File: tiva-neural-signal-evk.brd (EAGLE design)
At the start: 100 x 80 mm, 32 parts, among them IC1 TM4C123G, IC2 TLV70233, X1 USB, Y1 16MHz, Y2 32.768kHz

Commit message: added SD card in SPI mode
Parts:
- added C17: 0.1uF, rcl:C0603
- added X2: MICROSD, mor307:PUSH-PUSH
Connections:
- net +3V3: now also C17.1, X2.4
- net GND: now also C17.2, X2.6
- net PF0: now also X2.7
- net PF1: now also X2.3
- net PF2: now also X2.5
- net PF3: now also X2.2
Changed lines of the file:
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@@
 <attribute name="TP_SIGNAL_NAME" value="" x="-52.07" y="-106.68" size="1.778" layer="27" display="off"/>
 </element>
+<element name="X2" library="mor307" package="PUSH-PUSH" value="MICROSD" x="-67.31" y="-106.68"/>
+<element name="C17" library="rcl" package="C0603" value="0.1uF" x="-66.04" y="-110.49"/>
 </elements>
 <signals>
@@
 <contactref element="S1" pad="1"/>
 <contactref element="S1" pad="2"/>
+<contactref element="X2" pad="6"/>
+<contactref element="C17" pad="2"/>
+<wire x1="-63.66" y1="-102.38" x2="-65.19" y2="-110.49" width="0" layer="19" extent="1-1"/>
+<wire x1="-51.562" y1="-89.154" x2="-63.66" y2="-102.38" width="0" layer="19" extent="1-1"/>
 <wire x1="-44.958" y1="-89.154" x2="-51.562" y2="-89.154" width="0" layer="19" extent="1-1"/>
 <wire x1="-39.79" y1="-81.28" x2="-44.958" y2="-89.154" width="0" layer="19" extent="1-1"/>
@@
 <contactref element="+3V3" pad="TP"/>
 <contactref element="R3" pad="1"/>
+<contactref element="X2" pad="4"/>
+<contactref element="C17" pad="1"/>
+<wire x1="-61.46" y1="-102.38" x2="-66.89" y2="-110.49" width="0" layer="19" extent="1-1"/>
+<wire x1="-51.65" y1="-100.33" x2="-61.46" y2="-102.38" width="0" layer="19" extent="1-1"/>
 <wire x1="-39.79" y1="-85.09" x2="-51.65" y2="-100.33" width="0" layer="19" extent="1-1"/>
 <wire x1="-36.41" y1="-41.91" x2="-39.79" y2="-85.09" width="0" layer="19" extent="1-1"/>
@@
 <signal name="PF0">
 <contactref element="IC1" pad="28"/>
+<contactref element="X2" pad="7"/>
+<wire x1="-18.57" y1="2.02" x2="-64.76" y2="-102.38" width="0" layer="19" extent="1-1"/>
 </signal>
 <signal name="PF1">
 <contactref element="IC1" pad="29"/>
+<contactref element="X2" pad="3"/>
+<wire x1="-18.07" y1="2.02" x2="-60.36" y2="-102.38" width="0" layer="19" extent="1-1"/>
 </signal>
 <signal name="PF2">
 <contactref element="IC1" pad="30"/>
+<contactref element="X2" pad="5"/>
+<wire x1="-17.57" y1="2.02" x2="-62.56" y2="-102.38" width="0" layer="19" extent="1-1"/>
 </signal>
 <signal name="PF3">
 <contactref element="IC1" pad="31"/>
+<contactref element="X2" pad="2"/>
+<wire x1="-17.07" y1="2.02" x2="-59.26" y2="-102.38" width="0" layer="19" extent="1-1"/>
 </signal>
 <signal name="PF4">

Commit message: added 2-ch instrumentation amp w/ op-amp gain stage
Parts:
- added C18: 0.1uF, rcl:C0603
- added C19, C20, C21, C22, C23, C24: (no value), rcl:C0603
- added IC3: INA2332, mor307:TSSOP16
- added IC4, IC5: OPA2320, mor307:MSOP08
- added R4, R5, R6, R7: 100k, rcl:R0603
- added R8, R9: 1M, rcl:R0603
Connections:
- new net N$1: C20.2, IC3.7, R6.1, R7.1
- new net N$12: C19.2, IC3.13, R5.2, R8.1
- new net N$14: C21.1, IC4.2, R8.2
- new net N$15: C22.2, IC5.2, R9.2
- new net N$2: C22.1, IC3.10, IC5.1, R6.2
- new net N$3: C20.1, IC3.9, R7.2, R9.1
- new net N$4: C19.1, IC3.1, R4.1, R5.1
- new net N$5: C21.2, IC3.12, IC4.1, R4.2
- net +3V3: now also C18.1, C23.1, C24.1, IC3.11, IC3.14, IC3.8, IC4.8, IC5.8
- net GND: now also C18.2, C23.2, C24.2, IC3.4, IC4.4, IC5.4
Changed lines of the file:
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@@
 <element name="X2" library="mor307" package="PUSH-PUSH" value="MICROSD" x="-67.31" y="-106.68"/>
 <element name="C17" library="rcl" package="C0603" value="0.1uF" x="-66.04" y="-110.49"/>
+<element name="IC3" library="mor307" package="TSSOP16" value="INA2332" x="-73.66" y="-107.95"/>
+<element name="IC4" library="mor307" package="MSOP08" value="OPA2320" x="-73.66" y="-116.84"/>
+<element name="IC5" library="mor307" package="MSOP08" value="OPA2320" x="-73.66" y="-124.46"/>
+<element name="C18" library="rcl" package="C0603" value="0.1uF" x="-74.93" y="-130.81"/>
+<element name="R4" library="rcl" package="R0603" value="100k" x="-74.93" y="-135.89"/>
+<element name="R5" library="rcl" package="R0603" value="100k" x="-74.93" y="-140.97"/>
+<element name="C19" library="rcl" package="C0603" value="" x="-74.93" y="-146.05"/>
+<element name="R6" library="rcl" package="R0603" value="100k" x="-74.93" y="-149.86"/>
+<element name="R7" library="rcl" package="R0603" value="100k" x="-74.93" y="-154.94"/>
+<element name="C20" library="rcl" package="C0603" value="" x="-74.93" y="-160.02"/>
+<element name="R8" library="rcl" package="R0603" value="1M" x="-74.93" y="-163.83"/>
+<element name="C21" library="rcl" package="C0603" value="" x="-74.93" y="-168.91"/>
+<element name="R9" library="rcl" package="R0603" value="1M" x="-74.93" y="-172.72"/>
+<element name="C22" library="rcl" package="C0603" value="" x="-74.93" y="-177.8"/>
+<element name="C23" library="rcl" package="C0603" value="" x="-74.93" y="-181.61"/>
+<element name="C24" library="rcl" package="C0603" value="" x="-74.93" y="-185.42"/>
 </elements>
 <signals>
@@
 <contactref element="X2" pad="6"/>
 <contactref element="C17" pad="2"/>
+<contactref element="IC3" pad="4"/>
+<contactref element="C18" pad="2"/>
+<contactref element="IC4" pad="4"/>
+<contactref element="C23" pad="2"/>
+<contactref element="IC5" pad="4"/>
+<contactref element="C24" pad="2"/>
+<wire x1="-75.773" y1="-125.434" x2="-74.08" y2="-130.81" width="0" layer="19" extent="1-1"/>
+<wire x1="-75.773" y1="-117.814" x2="-75.773" y2="-125.434" width="0" layer="19" extent="1-1"/>
+<wire x1="-76.685" y1="-107.625" x2="-75.773" y2="-117.814" width="0" layer="19" extent="1-1"/>
+<wire x1="-65.19" y1="-110.49" x2="-76.685" y2="-107.625" width="0" layer="19" extent="1-1"/>
 <wire x1="-63.66" y1="-102.38" x2="-65.19" y2="-110.49" width="0" layer="19" extent="1-1"/>
 <wire x1="-51.562" y1="-89.154" x2="-63.66" y2="-102.38" width="0" layer="19" extent="1-1"/>
@@
 <wire x1="-29.21" y1="17.7499" x2="-25.92" y2="10.37" width="0" layer="19" extent="1-1"/>
 <wire x1="-16.48" y1="22.97" x2="-19.57" y2="13.22" width="0" layer="19" extent="1-1"/>
+<wire x1="-74.08" y1="-181.61" x2="-74.08" y2="-130.81" width="0" layer="19" extent="1-1"/>
+<wire x1="-74.08" y1="-185.42" x2="-74.08" y2="-181.61" width="0" layer="19" extent="1-1"/>
 </signal>
 <signal name="VBUS">
@@
 <contactref element="X2" pad="4"/>
 <contactref element="C17" pad="1"/>
+<contactref element="IC3" pad="11"/>
+<contactref element="C18" pad="1"/>
+<contactref element="IC3" pad="14"/>
+<contactref element="IC3" pad="8"/>
+<contactref element="C23" pad="1"/>
+<contactref element="IC4" pad="8"/>
+<contactref element="IC5" pad="8"/>
+<contactref element="C24" pad="1"/>
+<wire x1="-71.548" y1="-123.484" x2="-75.78" y2="-130.81" width="0" layer="19" extent="1-1"/>
+<wire x1="-71.548" y1="-115.864" x2="-71.548" y2="-123.484" width="0" layer="19" extent="1-1"/>
+<wire x1="-70.635" y1="-108.925" x2="-71.548" y2="-115.864" width="0" layer="19" extent="1-1"/>
+<wire x1="-70.635" y1="-106.975" x2="-70.635" y2="-108.925" width="0" layer="19" extent="1-1"/>
+<wire x1="-66.89" y1="-110.49" x2="-70.635" y2="-108.925" width="0" layer="19" extent="1-1"/>
+<wire x1="-76.685" y1="-110.225" x2="-70.635" y2="-108.925" width="0" layer="19" extent="1-1"/>
 <wire x1="-61.46" y1="-102.38" x2="-66.89" y2="-110.49" width="0" layer="19" extent="1-1"/>
 <wire x1="-51.65" y1="-100.33" x2="-61.46" y2="-102.38" width="0" layer="19" extent="1-1"/>
@@
 <wire x1="-19.57" y1="2.02" x2="-14.72" y2="5.87" width="0" layer="19" extent="1-1"/>
 <wire x1="-30.16" y1="20.3501" x2="-25.92" y2="10.87" width="0" layer="19" extent="1-1"/>
+<wire x1="-75.78" y1="-181.61" x2="-75.78" y2="-130.81" width="0" layer="19" extent="1-1"/>
+<wire x1="-75.78" y1="-185.42" x2="-75.78" y2="-181.61" width="0" layer="19" extent="1-1"/>
 </signal>
 <signal name="!HIB!">
@@
 <contactref element="IC1" pad="5"/>
 </signal>
+<signal name="N$4">
+<contactref element="IC3" pad="1"/>
+<contactref element="R4" pad="1"/>
+<contactref element="R5" pad="1"/>
+<contactref element="C19" pad="1"/>
+<wire x1="-75.78" y1="-140.97" x2="-75.78" y2="-146.05" width="0" layer="19" extent="1-1"/>
+<wire x1="-75.78" y1="-135.89" x2="-75.78" y2="-140.97" width="0" layer="19" extent="1-1"/>
+<wire x1="-76.685" y1="-105.675" x2="-75.78" y2="-135.89" width="0" layer="19" extent="1-1"/>
+</signal>
+<signal name="N$5">
+<contactref element="R4" pad="2"/>
+<contactref element="IC3" pad="12"/>
+<contactref element="IC4" pad="1"/>
+<contactref element="C21" pad="2"/>
+<wire x1="-74.08" y1="-135.89" x2="-74.08" y2="-168.91" width="0" layer="19" extent="1-1"/>
+<wire x1="-75.773" y1="-115.864" x2="-74.08" y2="-135.89" width="0" layer="19" extent="1-1"/>
+<wire x1="-70.635" y1="-108.275" x2="-75.773" y2="-115.864" width="0" layer="19" extent="1-1"/>
+</signal>
+<signal name="N$12">
+<contactref element="IC3" pad="13"/>
+<contactref element="R5" pad="2"/>
+<contactref element="C19" pad="2"/>
+<contactref element="R8" pad="1"/>
+<wire x1="-74.08" y1="-146.05" x2="-75.78" y2="-163.83" width="0" layer="19" extent="1-1"/>
+<wire x1="-74.08" y1="-140.97" x2="-74.08" y2="-146.05" width="0" layer="19" extent="1-1"/>
+<wire x1="-70.635" y1="-107.625" x2="-74.08" y2="-140.97" width="0" layer="19" extent="1-1"/>
+</signal>
+<signal name="N$1">
+<contactref element="IC3" pad="7"/>
+<contactref element="R6" pad="1"/>
+<contactref element="R7" pad="1"/>
+<contactref element="C20" pad="2"/>
+<wire x1="-75.78" y1="-154.94" x2="-74.08" y2="-160.02" width="0" layer="19" extent="1-1"/>
+<wire x1="-75.78" y1="-149.86" x2="-75.78" y2="-154.94" width="0" layer="19" extent="1-1"/>
+<wire x1="-76.685" y1="-109.575" x2="-75.78" y2="-149.86" width="0" layer="19" extent="1-1"/>
+</signal>
+<signal name="N$2">
+<contactref element="R6" pad="2"/>
+<contactref element="IC3" pad="10"/>
+<contactref element="IC5" pad="1"/>
+<contactref element="C22" pad="1"/>
+<wire x1="-74.08" y1="-149.86" x2="-75.78" y2="-177.8" width="0" layer="19" extent="1-1"/>
+<wire x1="-75.773" y1="-123.484" x2="-74.08" y2="-149.86" width="0" layer="19" extent="1-1"/>
+<wire x1="-70.635" y1="-109.575" x2="-75.773" y2="-123.484" width="0" layer="19" extent="1-1"/>
+</signal>
+<signal name="N$3">
+<contactref element="IC3" pad="9"/>
+<contactref element="R7" pad="2"/>
+<contactref element="C20" pad="1"/>
+<contactref element="R9" pad="1"/>
+<wire x1="-75.78" y1="-160.02" x2="-75.78" y2="-172.72" width="0" layer="19" extent="1-1"/>
+<wire x1="-74.08" y1="-154.94" x2="-75.78" y2="-160.02" width="0" layer="19" extent="1-1"/>
+<wire x1="-70.635" y1="-110.225" x2="-74.08" y2="-154.94" width="0" layer="19" extent="1-1"/>
+</signal>
+<signal name="N$14">
+<contactref element="IC4" pad="2"/>
+<contactref element="R8" pad="2"/>
+<contactref element="C21" pad="1"/>
+<wire x1="-74.08" y1="-163.83" x2="-75.78" y2="-168.91" width="0" layer="19" extent="1-1"/>
+<wire x1="-75.773" y1="-116.514" x2="-74.08" y2="-163.83" width="0" layer="19" extent="1-1"/>
+</signal>
+<signal name="N$15">
+<contactref element="IC5" pad="2"/>
+<contactref element="R9" pad="2"/>
+<contactref element="C22" pad="2"/>
+<wire x1="-74.08" y1="-172.72" x2="-74.08" y2="-177.8" width="0" layer="19" extent="1-1"/>
+<wire x1="-75.773" y1="-124.134" x2="-74.08" y2="-172.72" width="0" layer="19" extent="1-1"/>
+</signal>
 </signals>

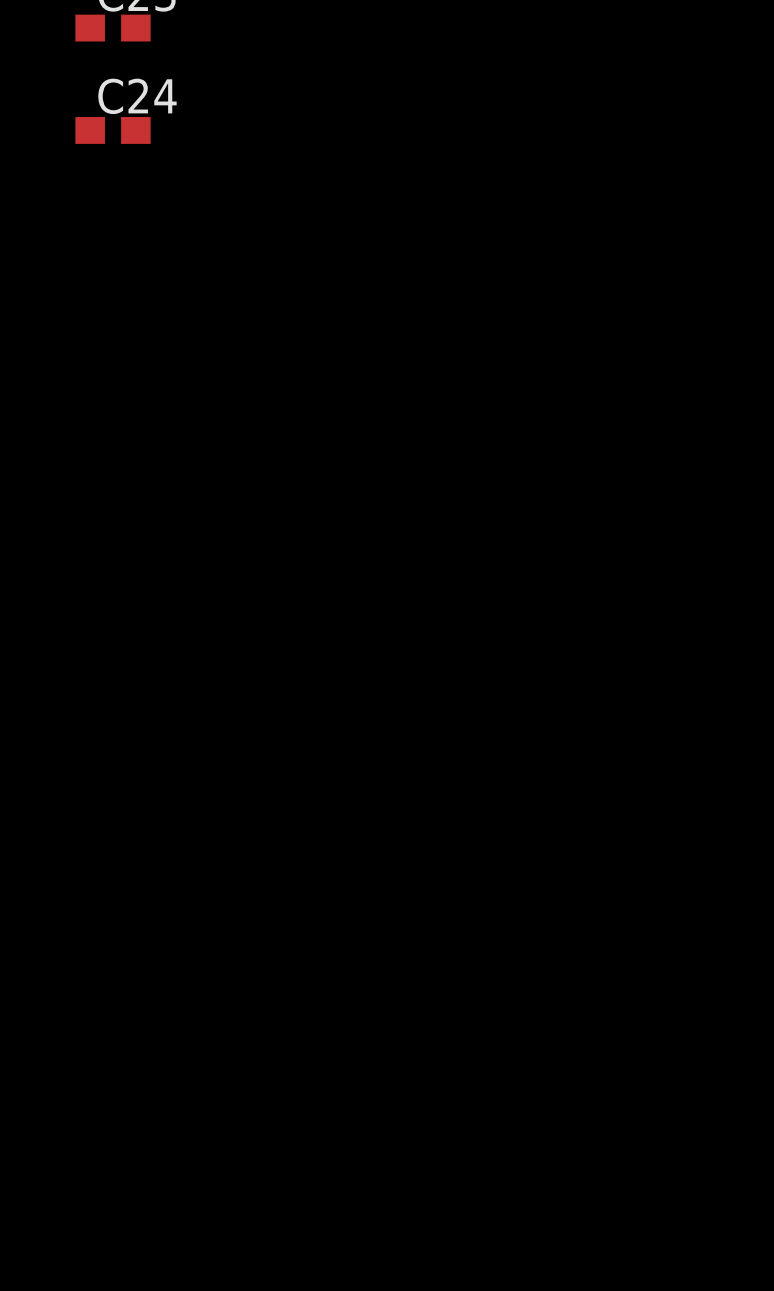
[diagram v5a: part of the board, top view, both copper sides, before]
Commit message: added another 2-ch instrumentation amplifer
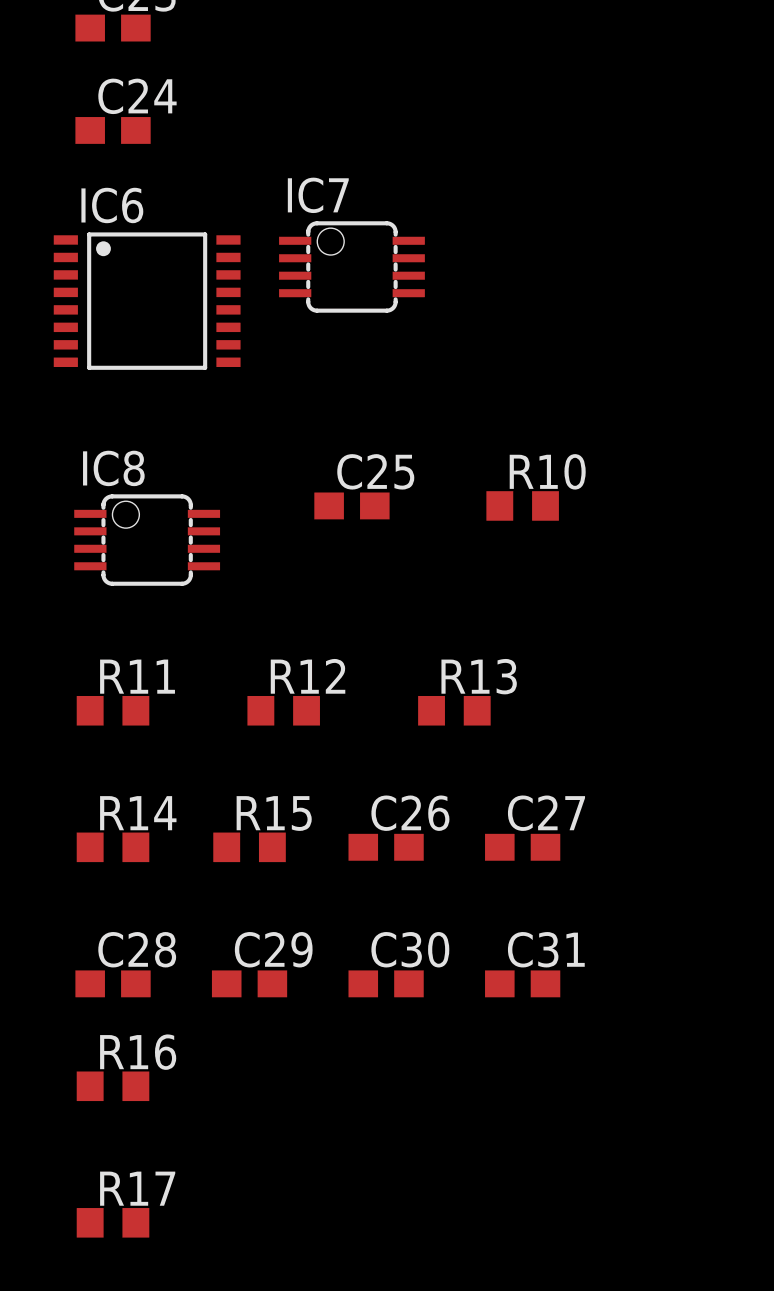
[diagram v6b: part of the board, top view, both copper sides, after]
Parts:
- added C25: 0.1uF, rcl:C0603
- added C26, C27, C28, C29, C30, C31: (no value), rcl:C0603
- added IC6: INA2332, mor307:TSSOP16
- added IC7, IC8: OPA2320, mor307:MSOP08
- added R10, R11, R12, R13, R16, R17: 100k, rcl:R0603
- added R14, R15: 1M, rcl:R0603
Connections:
- new net N$13: C27.2, IC6.7, R12.1, R13.1
- new net N$16: C29.1, IC6.10, IC8.1, R12.2
- new net N$17: C28.1, IC7.2, R14.2
- new net N$18: C29.2, IC8.2, R15.2
- new net VOA1: C19.2, C26.2, IC3.13, IC6.13, R11.2, R14.1, R5.2, R8.1
- new net VOB1: C20.1, C27.1, IC3.9, IC6.9, R13.2, R15.1, R7.2, R9.1
- new net VREF: IC4.3, IC5.3, IC7.3, IC8.3, R16.1, R17.2
- net +3V3: now also C25.1, C30.1, C31.1, IC6.11, IC6.14, IC6.8, IC7.8, IC8.8, R16.2
- net GND: now also C25.2, C30.2, C31.2, IC6.4, IC7.4, IC8.4, R17.1
- net N$12: now also C28.2, IC6.12, IC7.1, R10.2; no longer C19.2, IC3.13, R5.2, R8.1
- net N$3: now also C26.1, IC6.1, R10.1, R11.1; no longer C20.1, IC3.9, R7.2, R9.1

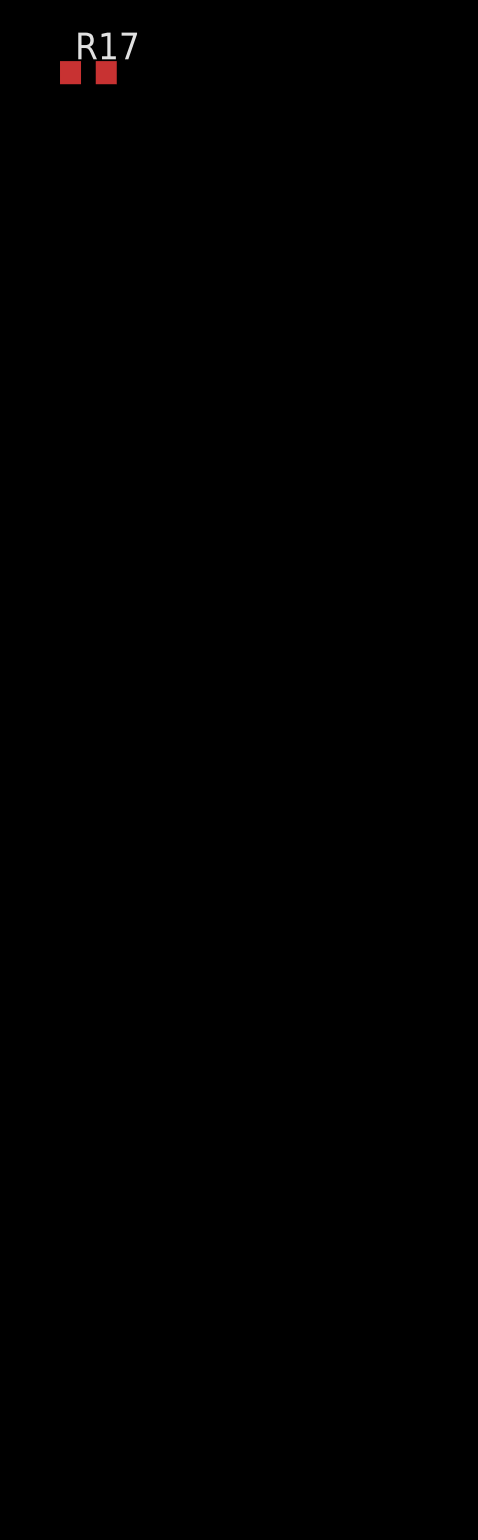
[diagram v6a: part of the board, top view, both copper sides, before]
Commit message: completed amplifier stage design
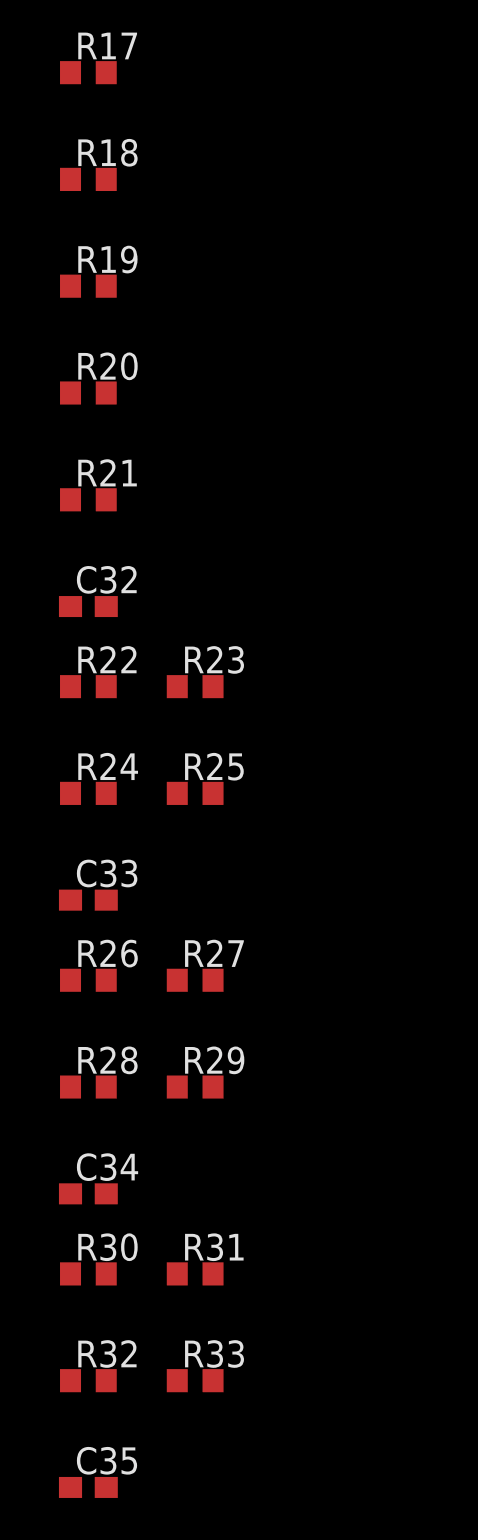
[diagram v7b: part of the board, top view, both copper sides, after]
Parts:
- added C32, C33, C34, C35: (no value), rcl:C0603
- added R18, R19, R20, R21, R22, R23, R24, R25, R26, R27, R28, R29, R30, R31, R32, R33: 1M, rcl:R0603
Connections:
- new net N$19: IC4.5, R18.1, R19.2
- new net N$20: C32.2, IC4.6, R20.1, R21.2
- new net N$21: C32.1, IC4.7, R21.1
- new net N$22: IC7.5, R26.1, R27.2
- new net N$23: IC5.5, R22.1, R23.2
- new net N$24: C33.2, IC5.6, R24.1, R25.2
- new net N$25: C33.1, IC5.7, R25.1
- new net N$26: C34.2, IC7.6, R28.1, R29.2
- new net N$27: C34.1, IC7.7, R29.1
- new net N$28: IC8.5, R30.1, R31.2
- new net N$29: C35.2, IC8.6, R32.1, R33.2
- new net N$30: C35.1, IC8.7, R33.1
- new net VOA2: C26.2, IC6.13, R11.2, R14.1, R28.2
- new net VOB2: C27.1, IC6.9, R13.2, R15.1, R32.2
- net +3V3: now also R18.2, R22.2, R26.2, R30.2
- net GND: now also R19.1, R23.1, R27.1, R31.1
- net VOA1: now also R20.2; no longer C26.2, IC6.13, R11.2, R14.1
- net VOB1: now also R24.2; no longer C27.1, IC6.9, R13.2, R15.1

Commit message: laid out components
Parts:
- added U$1, U$2, U$3, U$4: 2_PIN_HEADERHEADER, ng:SMT_PINS_2
- moved C33 341.4 mm to (38.7, 56.5), turned to 180 degrees
- moved C32 334.2 mm to (38.7, 62.9), turned to 180 degrees
- moved R24 334.0 mm to (34.3, 55.2), turned to 270 degrees
- moved R25 333.8 mm to (38.7, 55.2), turned to 180 degrees
- moved R22 329.3 mm to (40.0, 53.3), flipped to the bottom, turned to 180 degrees
- moved R21 328.3 mm to (38.7, 61.6), turned to 180 degrees
- moved R23 326.7 mm to (37.5, 53.3), flipped to the bottom, turned to 180 degrees
- moved R20 319.6 mm to (34.3, 59.1), turned to 270 degrees
- moved R19 316.5 mm to (37.5, 59.7), flipped to the bottom, turned to 180 degrees
- moved R18 312.7 mm to (40.0, 59.7), flipped to the bottom, turned to 180 degrees
- moved C23 265.0 mm to (38.7, 57.8), flipped to the bottom
- moved IC8 262.8 mm to (17.8, 45.7)
- moved C24 262.7 mm to (38.7, 51.4), flipped to the bottom
- moved C25 260.2 mm to (7.62, 50.2), flipped to the bottom
- moved IC7 257.8 mm to (17.8, 53.3)
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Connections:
- net N$21 renamed V1A
- net N$25 renamed V1B
- net N$27 renamed V2A
- net N$30 renamed V2B
- new net N$21: IC3.2, U$1.1
- new net N$25: IC3.3, U$1.2
- new net N$27: IC6.6, U$4.1
- new net N$30: IC6.5, U$4.2
- new net N$31: IC3.5, U$2.2
- new net N$32: IC3.6, U$2.1
- new net N$33: IC6.2, U$3.1
- new net N$34: IC6.3, U$3.2
- net N$6: now also Y2.X1; no longer Y2.X2
- net N$8: now also Y2.X2; no longer Y2.X1
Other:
- board size 100 x 80 mm -> 50.8 x 69.8 mm
